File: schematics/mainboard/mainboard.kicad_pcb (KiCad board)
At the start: 4 copper layers, 82 x 150 mm, 7 parts, among them J1 SD_Card_Receptacle, J2 Conn_02x20_Odd_Even_MountingP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, J3 USB_C_Receptacle_USB2.0_16P, P1 1-1473005-4, U1 TLV75801PDBV

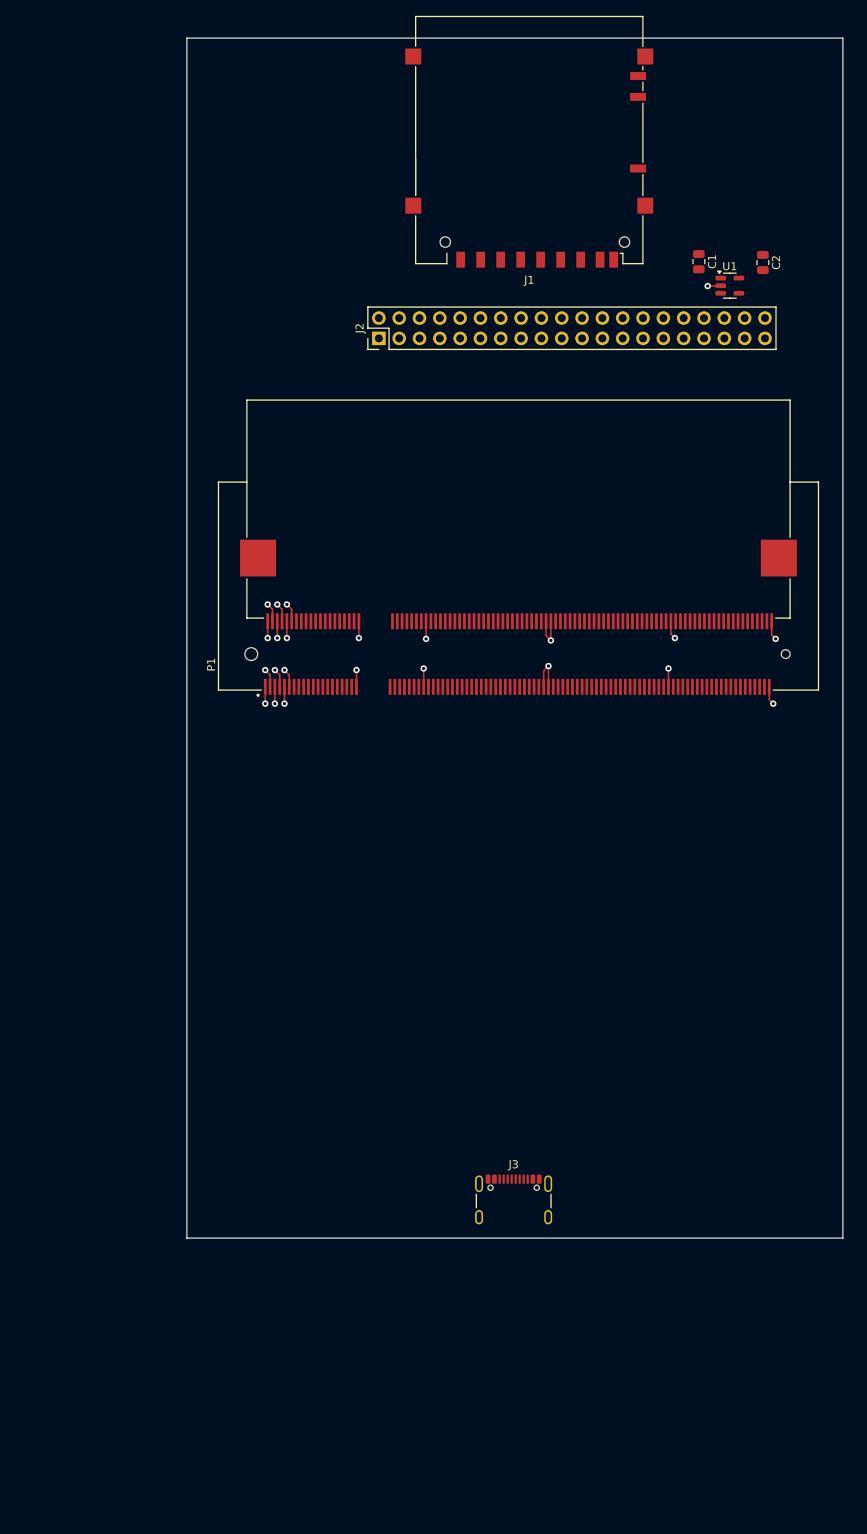
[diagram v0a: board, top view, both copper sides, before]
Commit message: Begun SRAM symbol. Reorganized a bit on mainboard.
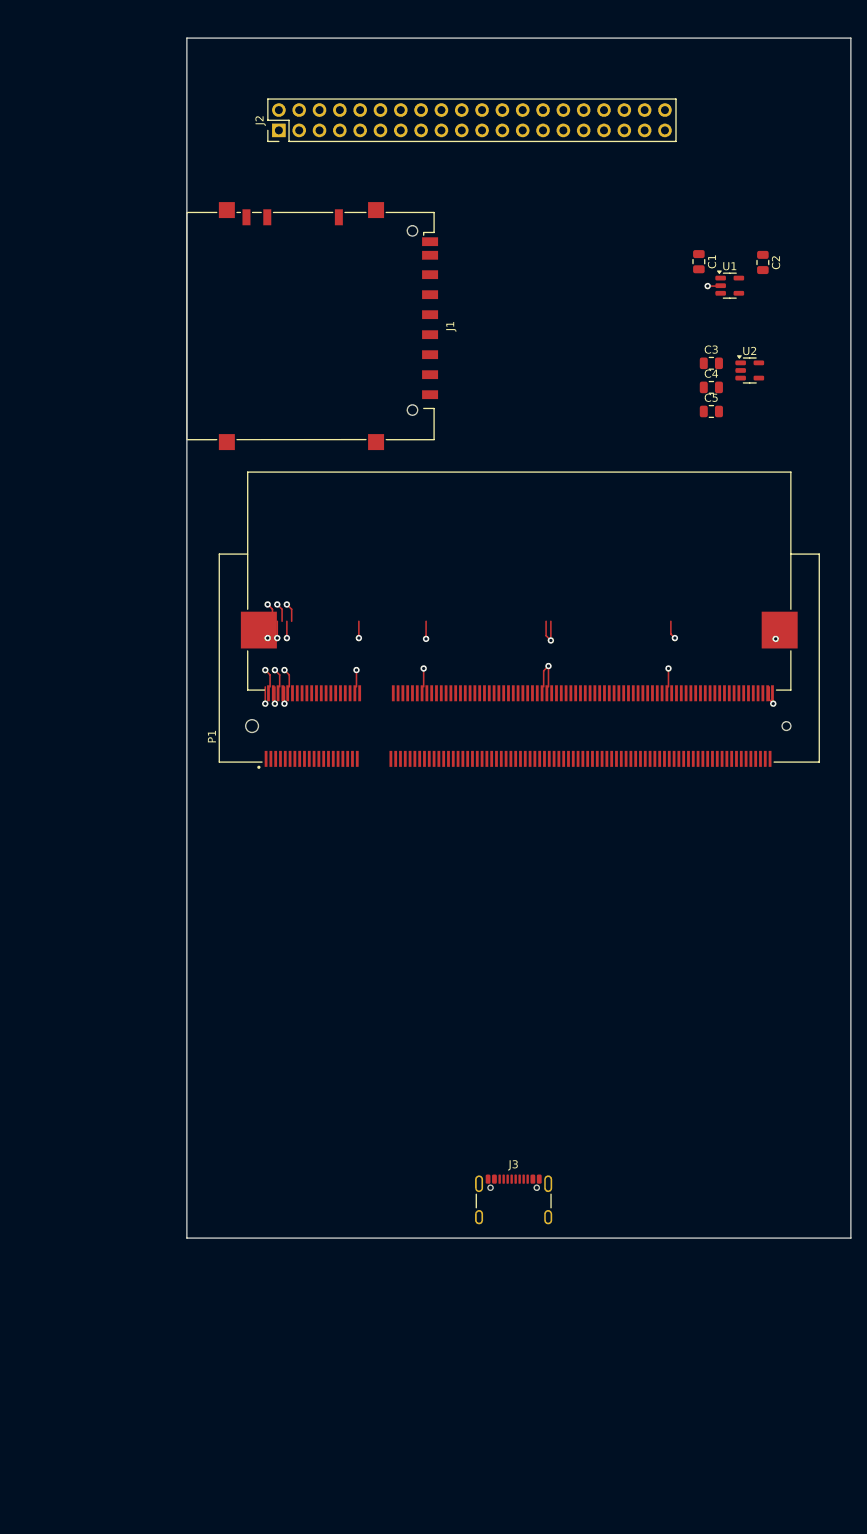
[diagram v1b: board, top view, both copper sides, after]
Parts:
- added C3: C, Capacitor_SMD:C_0805_2012Metric, F.Cu at (180.6, 140.7)
- added C4: C, Capacitor_SMD:C_0805_2012Metric, F.Cu at (180.6, 143.7)
- added C5: C, Capacitor_SMD:C_0805_2012Metric, F.Cu at (180.6, 146.7)
- added U2: TLV75801PDBV, Package_TO_SOT_SMD:SOT-23-5, F.Cu at (185.4, 141.6)
- moved J1 35.9 mm to (130.4, 136.0), turned to -90 degrees
- moved J2 28.8 mm to (126.5, 111.5)
- moved P1 9.00 mm to (156.6, 186.0)
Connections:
- J1 pad 3: Net-(J1-VSS-Pad3) -> GND
- J1 pad 4: unconnected-(J1-VDD-Pad4) -> 3V3_SD
- J1 pad 6: Net-(J1-VSS-Pad3) -> GND
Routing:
- net GND: track 43.5 -> 25.6 mm
- net 5V5: track 13.3 -> 24.6 mm
- net unconnected-(P1-Pad54): track 0.00 -> 2.30 mm
- net LCD_R1: track 0.00 -> 2.30 mm
- net unconnected-(P1-Pad38): track 0.00 -> 2.10 mm
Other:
- board size 82 x 150 mm -> 83 x 150 mm

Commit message: Much work on mainboard.
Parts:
- added C10: C, Capacitor_SMD:C_0805_2012Metric, F.Cu at (151.0, 219.5)
- added C11: C, Capacitor_SMD:C_0805_2012Metric, F.Cu at (151.1, 236.1)
- added C12: C, Capacitor_SMD:C_0805_2012Metric, F.Cu at (172.1, 238.7)
- added C13: C, Capacitor_SMD:C_0805_2012Metric, F.Cu at (172.3, 221.9)
- added C14: C, Capacitor_SMD:C_0805_2012Metric, F.Cu at (151.1, 229.0)
- added C6: C, Capacitor_SMD:C_0805_2012Metric, F.Cu at (140.8, 252.8)
- added C7: 1u, Capacitor_SMD:C_0805_2012Metric, F.Cu at (152.5, 253.0)
- added C8: 1u, Capacitor_SMD:C_0805_2012Metric, F.Cu at (122.5, 238.5)
- added C9: 1u, Capacitor_SMD:C_0805_2012Metric, F.Cu at (122.5, 241.5)
- added R1: 33, Resistor_SMD:R_0805_2012Metric_Pad1.20x1.40mm_HandSolder, F.Cu at (157.0, 261.6)
- added R2: 33, Resistor_SMD:R_0805_2012Metric_Pad1.20x1.40mm_HandSolder, F.Cu at (154.6, 261.6)
- added R3: 1k, Resistor_SMD:R_0805_2012Metric_Pad1.20x1.40mm_HandSolder, F.Cu at (122.7, 235.5)
- added REF**: MountingHole_3.2mm_M3_DIN965, MountingHole:MountingHole_3.2mm_M3_DIN965, F.Cu at (118.6, 155.8)
- added REF**: MountingHole_3.2mm_M3_DIN965, MountingHole:MountingHole_3.2mm_M3_DIN965, F.Cu at (176.4, 155.6)
- added REF**: MountingHole_3.2mm_M3_DIN965, MountingHole:MountingHole_3.2mm_M3_DIN965, F.Cu at (176.7, 106.9)
- added REF**: MountingHole_3.2mm_M3_DIN965, MountingHole:MountingHole_3.2mm_M3_DIN965, F.Cu at (118.3, 107.0)
- added TP_3V3_LCD1: TP_3V3_LCD, TestPoint:TestPoint_Pad_D1.5mm, F.Cu at (189.0, 124.0)
- added TP_3V3_SD1: TP_3V3_SD, TestPoint:TestPoint_Pad_D1.5mm, F.Cu at (129.0, 159.0)
- added TP_5V0: TP_5V0, TestPoint:TestPoint_Pad_D1.5mm, F.Cu at (120.0, 216.0)
- added TP_VBUS1: TP_VBUS, TestPoint:TestPoint_Pad_D1.5mm, F.Cu at (128.0, 231.0)
- added U3: MAX3421EETJ_T, MAX:QFN50P500X500X80-33N, F.Cu at (146.2, 252.6)
- added U4: ~, Package_SO:TSOP-II-54_22.2x10.16mm_P0.8mm, F.Cu at (161.5, 229.1)
- added U5: BQ24040DSQR, BQ24040DSQR:SON40P200X200X80-11N, F.Cu at (129.0, 237.1)
- added U6: TPS63002, Package_SON:Texas_DRC0010J_ThermalVias, F.Cu at (123.2, 222.5)
- moved U2 57.7 mm to (128.8, 153.0)
- moved C3 57.5 mm to (124.2, 152.0)
- moved C4 47.8 mm to (133.4, 152.0), turned to 180 degrees
- moved C5 46.2 mm to (136.6, 132.4), turned to 90 degrees
- moved J3 24.4 mm to (156.2, 270.7)
- moved U1 14.1 mm to (184.6, 117.0)
- moved J1 13.5 mm to (117.5, 132.5)
- moved C2 12.3 mm to (189.3, 116.0), turned to 180 degrees
- moved C1 12.0 mm to (179.9, 116.0), turned to 0 degrees
- moved P1 8.91 mm to (156.8, 194.9)
- moved J2 4.53 mm to (123.4, 108.2)
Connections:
- P1 pad 10: 5V5 -> 5V0
- P1 pad 101: unconnected-(P1-Pad101) -> SRAM_D14
- P1 pad 103: unconnected-(P1-Pad103) -> SRAM_D13
- P1 pad 109: UART_RX -> SRAM_D12
- P1 pad 111: UART_TX -> SRAM_D11
- P1 pad 113: unconnected-(P1-Pad113) -> SRAM_D10
- P1 pad 115: unconnected-(P1-Pad115) -> SRAM_D9
- P1 pad 117: unconnected-(P1-Pad117) -> SRAM_D8
- P1 pad 119: unconnected-(P1-Pad119) -> SRAM_A5
- P1 pad 12: 5V5 -> 5V0
- P1 pad 121: unconnected-(P1-Pad121) -> SRAM_A6
- P1 pad 123: unconnected-(P1-Pad123) -> SRAM_A7
- P1 pad 125: unconnected-(P1-Pad125) -> SRAM_A8
- P1 pad 127: unconnected-(P1-Pad127) -> SRAM_A9
- P1 pad 129: unconnected-(P1-Pad129) -> ~{SRAM_OE}
- P1 pad 131: unconnected-(P1-Pad131) -> SRAM_A10
- P1 pad 133: unconnected-(P1-Pad133) -> SRAM_A11
- P1 pad 135: unconnected-(P1-Pad135) -> SRAM_A12
- P1 pad 137: unconnected-(P1-Pad137) -> SRAM_A13
- P1 pad 139: unconnected-(P1-Pad139) -> SRAM_A14
- P1 pad 141: unconnected-(P1-Pad141) -> SRAM_D7
- P1 pad 143: unconnected-(P1-Pad143) -> SRAM_D6
- P1 pad 145: unconnected-(P1-Pad145) -> SRAM_D5
- P1 pad 147: unconnected-(P1-Pad147) -> SRAM_D4
- P1 pad 2: 5V5 -> 5V0
- P1 pad 4: 5V5 -> 5V0
- P1 pad 46: SD_DAT3 -> SD_CLK
- P1 pad 48: SD_DAT2 -> SD_CMD
- P1 pad 50: SD_CLK -> SD_DAT3
- P1 pad 52: SD_CMD -> SD_DAT2
- P1 pad 57: unconnected-(P1-Pad57) -> USB_HCI_INT
- P1 pad 59: unconnected-(P1-Pad59) -> USB_HCI_MOSI
- P1 pad 6: 5V5 -> 5V0
- P1 pad 61: unconnected-(P1-Pad61) -> USB_HCI_MISO
- P1 pad 63: unconnected-(P1-Pad63) -> ~{USB_HCI_SS}
- P1 pad 65: unconnected-(P1-Pad65) -> USB_HCI_SCLK
- P1 pad 67: unconnected-(P1-Pad67) -> ~{USB_HCI_RESET}
- P1 pad 69: unconnected-(P1-Pad69) -> SRAM_D3
- P1 pad 71: unconnected-(P1-Pad71) -> SRAM_D2
- P1 pad 73: unconnected-(P1-Pad73) -> SRAM_D1
- P1 pad 75: unconnected-(P1-Pad75) -> SRAM_D0
- P1 pad 77: unconnected-(P1-Pad77) -> SRAM_A15
- P1 pad 79: unconnected-(P1-Pad79) -> SRAM_A16
- P1 pad 8: 5V5 -> 5V0
- P1 pad 81: unconnected-(P1-Pad81) -> SRAM_A17
- P1 pad 83: unconnected-(P1-Pad83) -> SRAM_A18
- P1 pad 85: unconnected-(P1-Pad85) -> SRAM_A19
- P1 pad 87: unconnected-(P1-Pad87) -> ~{SRAM_WE}
- P1 pad 89: unconnected-(P1-Pad89) -> SRAM_A0
- P1 pad 91: unconnected-(P1-Pad91) -> SRAM_A1
- P1 pad 93: unconnected-(P1-Pad93) -> SRAM_A2
- P1 pad 95: unconnected-(P1-Pad95) -> SRAM_A3
- P1 pad 97: unconnected-(P1-Pad97) -> SRAM_A4
- P1 pad 99: unconnected-(P1-Pad99) -> SRAM_D15
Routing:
- net 5V5: track 24.6 -> 0.00 mm, vias 6 -> 0
- net 5V0: track 0.00 -> 13.3 mm, vias 0 -> 6
- net GND: track 25.6 -> 36.4 mm, vias 17 -> 16
- net unconnected-(P1-Pad104): track 0.00 -> 5.45 mm
- net unconnected-(P1-Pad54): track 2.30 -> 0.00 mm
- net LCD_R1: track 2.30 -> 0.00 mm
- net unconnected-(P1-Pad38): track 2.10 -> 0.00 mm
- added copper zone on In2.Cu, net 5V0
- removed copper zone on In2.Cu, net 5V5
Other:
- board size 83 x 150 mm -> 96 x 175 mm
- board text added: "Incorrect FP"

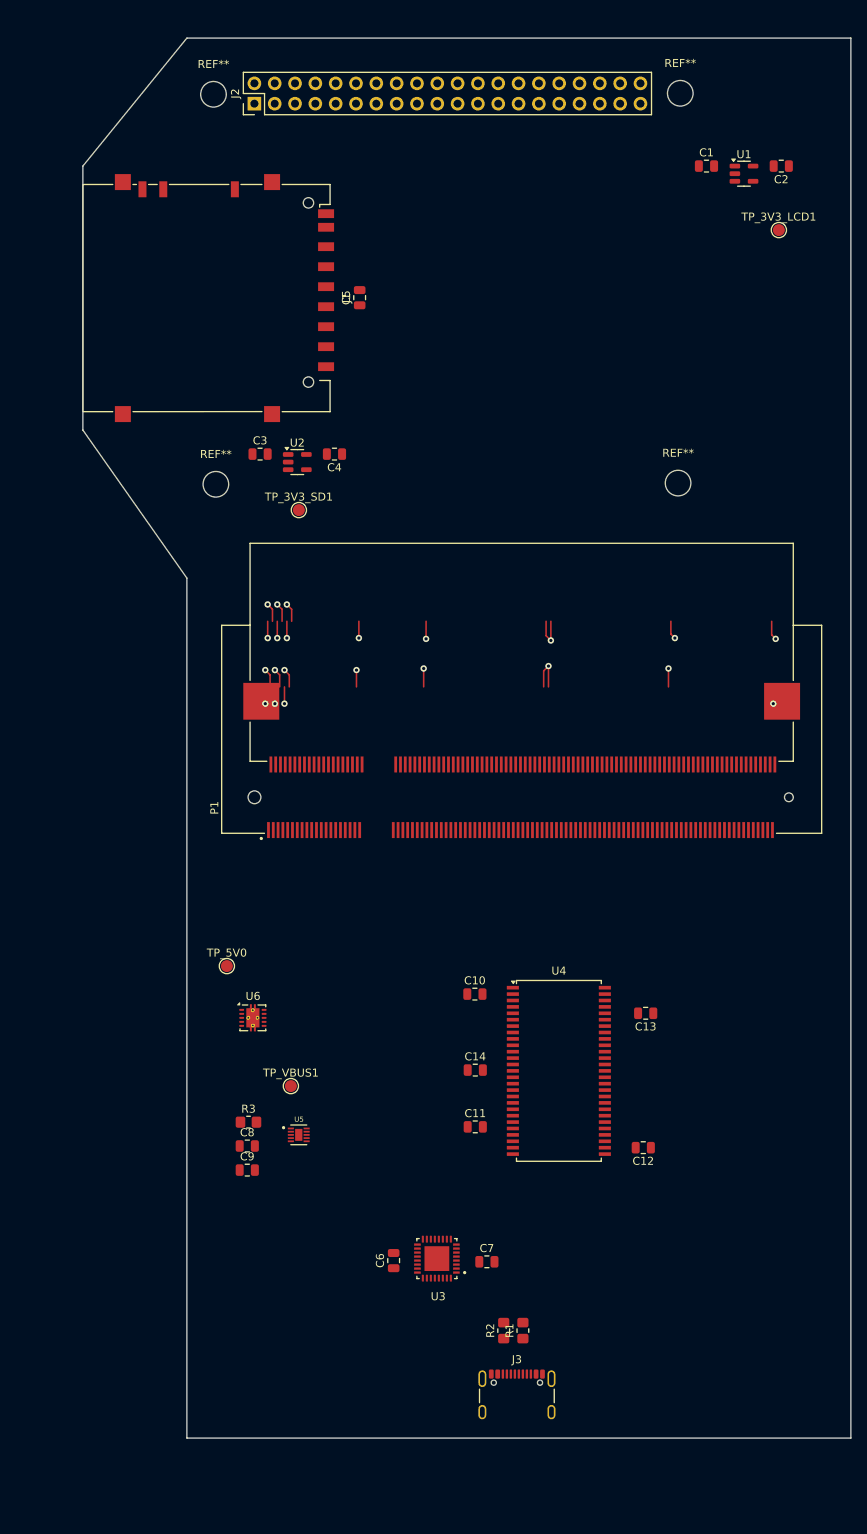
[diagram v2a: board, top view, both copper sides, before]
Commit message: Layed out some PCB tracks.
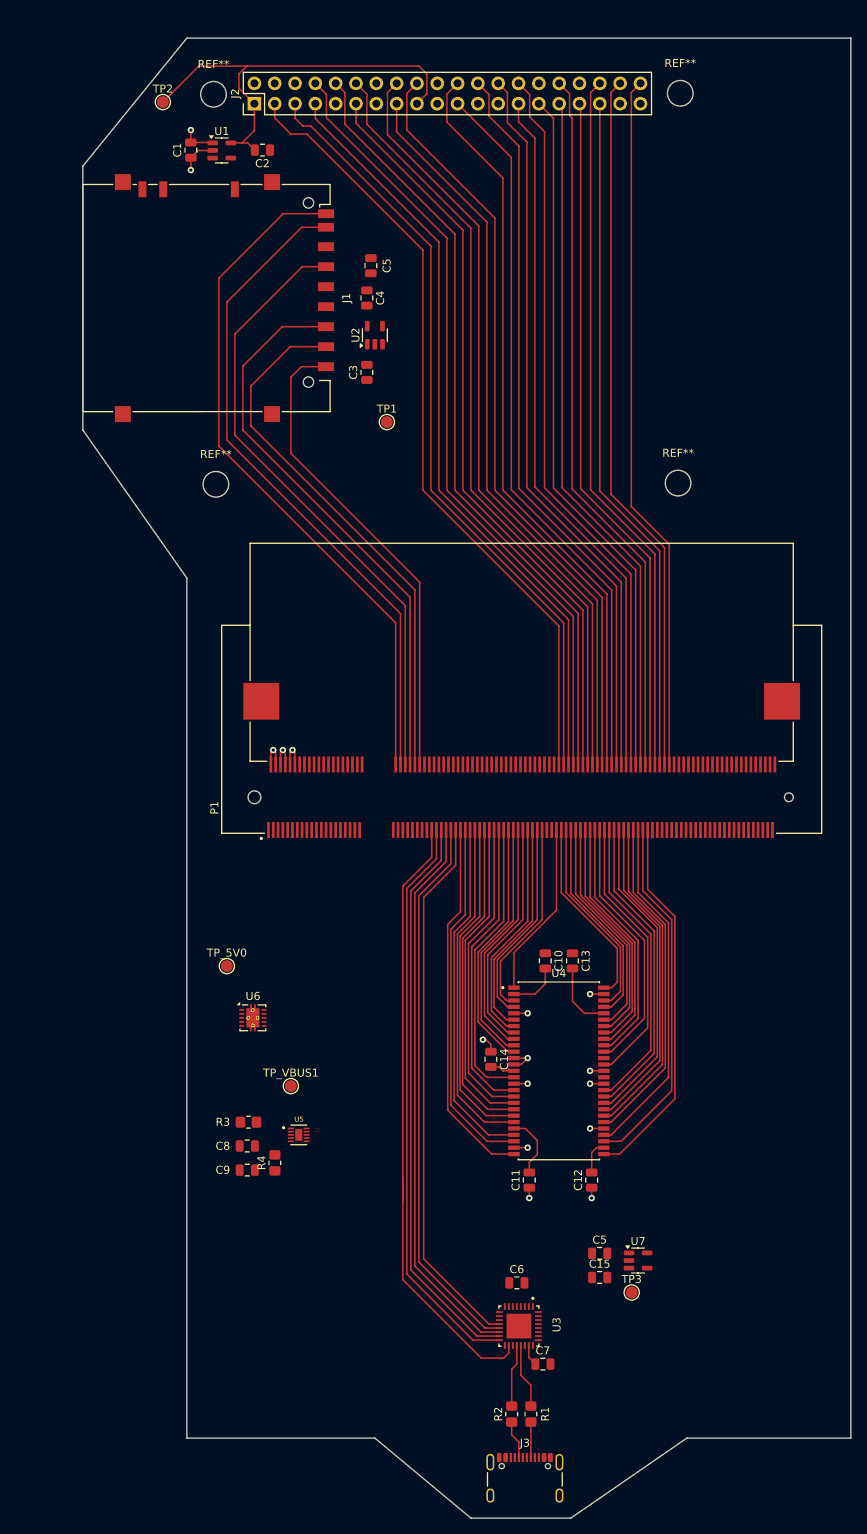
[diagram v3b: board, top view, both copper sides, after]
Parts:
- added C15: C, Capacitor_SMD:C_0805_2012Metric, F.Cu at (166.6, 254.9)
- added C5: C, Capacitor_SMD:C_0805_2012Metric, F.Cu at (166.6, 251.9)
- added R4: 2k, Resistor_SMD:R_0805_2012Metric_Pad1.20x1.40mm_HandSolder, F.Cu at (126.0, 240.6)
- added TP3: TP_3V3, TestPoint:TestPoint_Pad_D1.5mm, F.Cu at (170.6, 256.8)
- added U7: TLV75801PDBV, Package_TO_SOT_SMD:SOT-23-5, F.Cu at (171.4, 252.8)
- R3: value 1k -> 540
- U4: footprint Package_SO:TSOP-II-54_22.2x10.16mm_P0.8mm -> libraries:SOP80P1176X120-54N
- moved TP2 78.6 mm to (112.0, 108.0)
- moved U1 65.3 mm to (119.4, 114.0)
- moved C2 64.9 mm to (124.5, 114.0)
- moved C1 64.5 mm to (115.5, 114.0), turned to 90 degrees
- moved C4 19.9 mm to (137.5, 132.5), turned to -90 degrees
- moved U2 18.6 mm to (138.5, 137.1), turned to 90 degrees
- moved C3 16.8 mm to (137.5, 141.8), turned to 90 degrees
- moved C6 15.6 mm to (156.2, 255.6), turned to 0 degrees
- moved TP1 15.6 mm to (140.0, 148.0)
- moved C7 14.6 mm to (159.5, 265.8)
- moved U3 13.3 mm to (156.5, 261.0), turned to -90 degrees
- moved C13 11.3 mm to (163.2, 215.3), turned to -90 degrees
- moved R1 10.5 mm to (158.0, 272.0)
- moved R2 10.5 mm to (155.6, 272.0)
- moved J3 10.5 mm to (157.2, 281.1)
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- renumbered TP_3V3_SD1 to TP1, TP_3V3_LCD1 to TP2
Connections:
- C10 pad 2: 3V3_SD -> 3V3
- C11 pad 2: 3V3_SD -> 3V3
- C12 pad 2: 3V3_SD -> 3V3
- C13 pad 2: 3V3_SD -> 3V3
- C14 pad 2: 3V3_SD -> 3V3
- C6 pad 1: 3V3_SD -> 3V3
- C7 pad 1: 3V3_SD -> 3V3
- U3 pad 2: 3V3_SD -> 3V3
- U3 pad 23: 3V3_SD -> 3V3
- U4 pad 14: 3V3_SD -> 3V3
- U4 pad 2: 3V3_SD -> 3V3
- U4 pad 23: 3V3_SD -> 3V3
- U4 pad 29: 3V3_SD -> 3V3
- U4 pad 50: 3V3_SD -> 3V3
- U5 pad 11: unconnected-(U5-EXP-Pad11) -> GND
- U5 pad 4: unconnected-(U5-PRETERM-Pad4) -> Net-(U5-PRETERM)
- U5 pad 7: unconnected-(U5-ISET2-Pad7) -> GND
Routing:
- net LCD_G2: track 0.00 -> 98.5 mm
- net LCD_VSYNC: track 0.00 -> 98.5 mm
- net LCD_G3: track 0.00 -> 97.7 mm
- net LCD_CS: track 0.00 -> 97.1 mm
- net LCD_HSYNC: track 0.00 -> 97.1 mm
- net LCD_R3: track 0.00 -> 96.2 mm
- net LCD_R4: track 0.00 -> 95.8 mm
- net LCD_B0: track 0.00 -> 95.7 mm
- net LCD_G5: track 0.00 -> 94.3 mm
- net LCD_R5: track 0.00 -> 94.0 mm
- net LCD_R2: track 0.00 -> 93.0 mm
- net LCD_B4: track 0.00 -> 92.3 mm
- net LCD_B3: track 0.00 -> 91.5 mm
- net LCD_ENABLE: track 0.00 -> 91.0 mm
- net LCD_B5: track 0.00 -> 90.6 mm
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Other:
- board size 96 x 175 mm -> 96 x 185 mm
- board text removed: "Incorrect FP"
